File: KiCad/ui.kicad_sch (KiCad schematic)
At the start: 42 parts, among them SW1 PEC11R-4215F-S0024, SW2 PEC11R-4215F-S0024, U10 BME280, U11 SN74HC14PWR, U12 LM35DGS, U8 SN74AHCT244DBR, U9 24LC256-I_ST

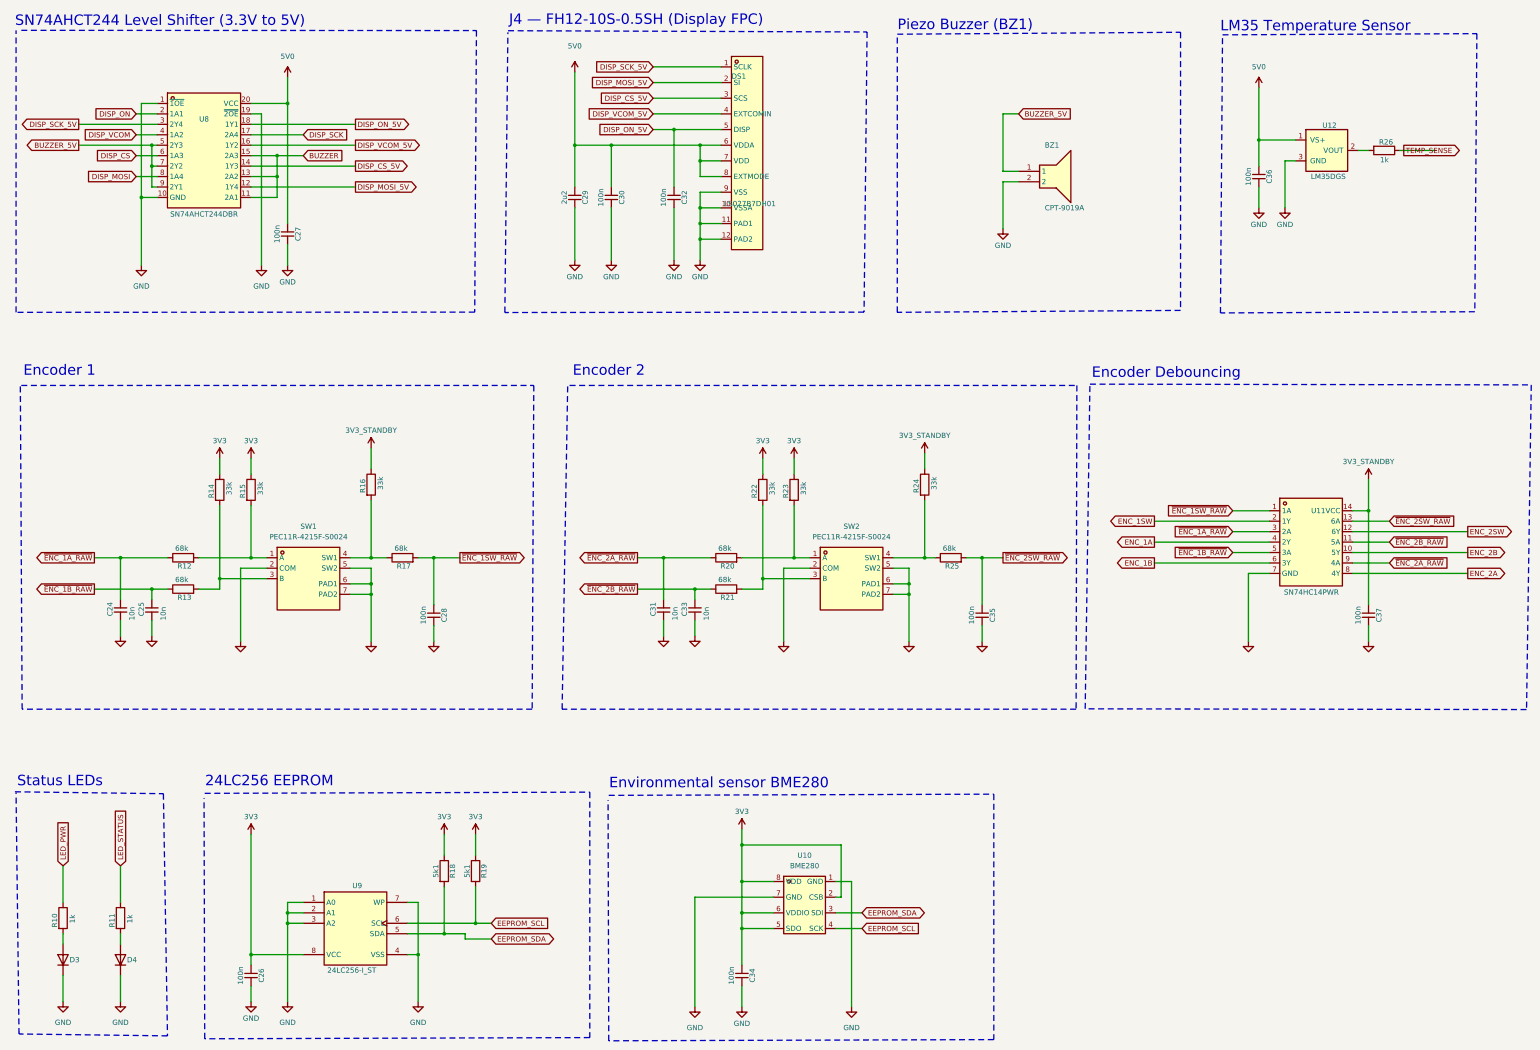
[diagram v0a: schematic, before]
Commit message: Symbols and board updated to match library
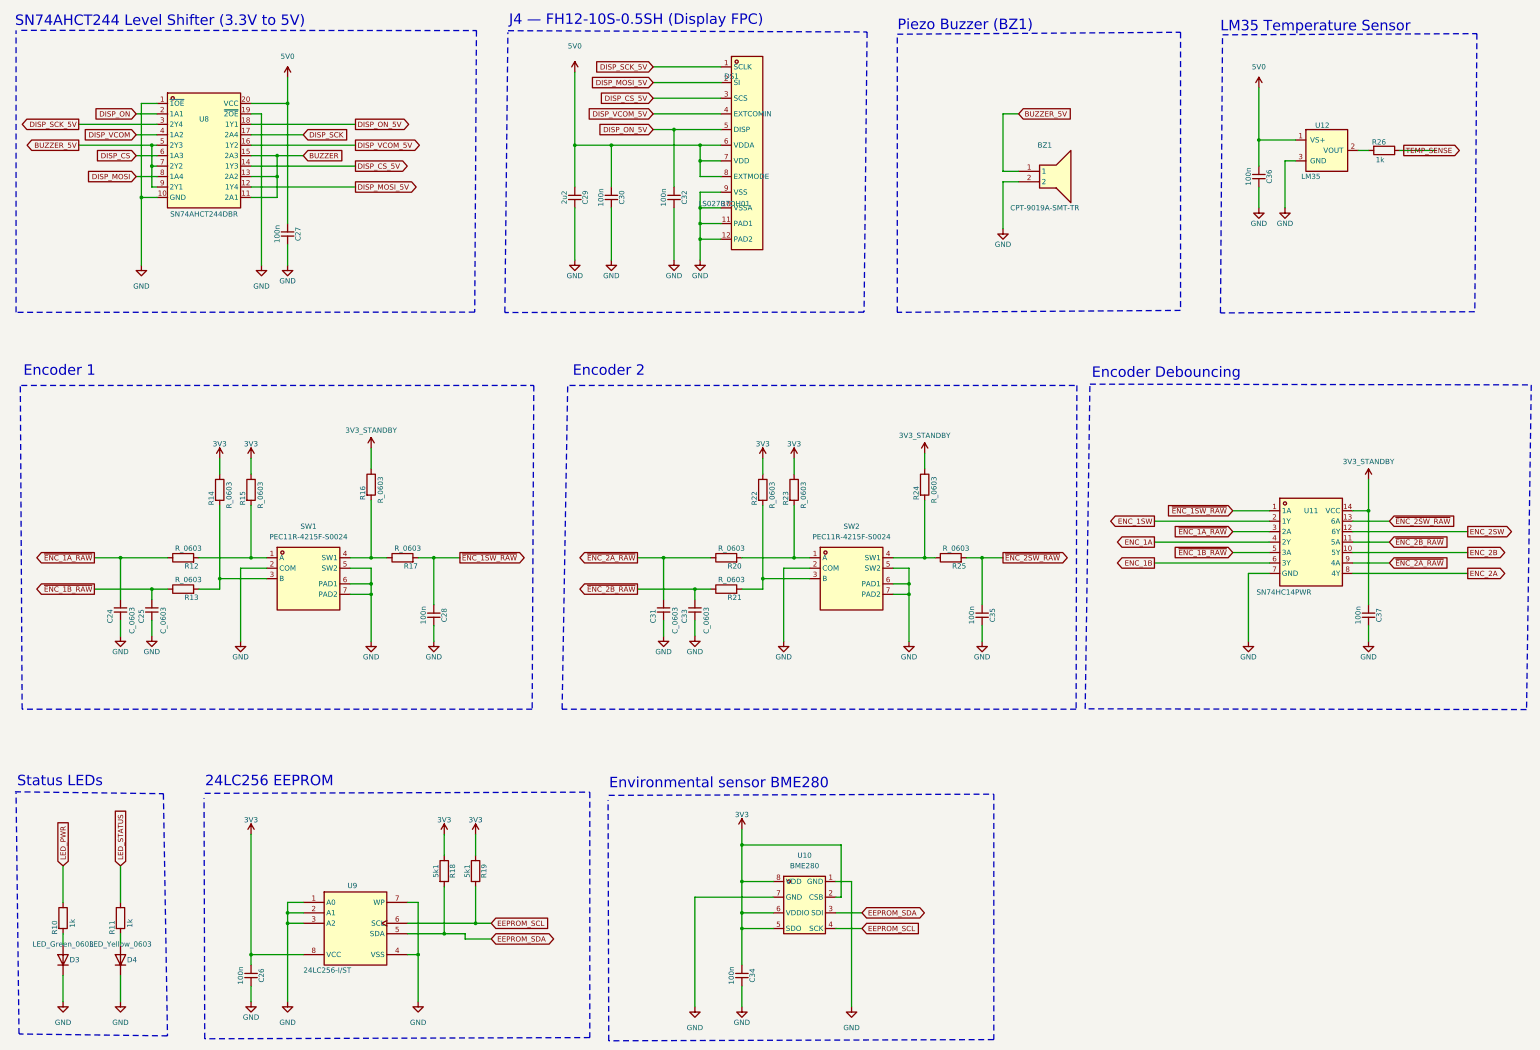
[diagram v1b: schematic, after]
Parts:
- BZ1: value CPT-9019A -> CPT-9019A-SMT-TR
- C24, C25, C31, C33: value 10n -> C_0603
- D4: value LED_Green_0603 -> LED_Yellow_0603
- R12, R13, R17, R20, R21, R25: value 68k -> R_0603
- R14, R15, R16, R22, R23, R24: value 33k -> R_0603
- U12: value LM35DGS -> LM35
- U9: value 24LC256-I_ST -> 24LC256-I/ST

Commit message: Remaining resistors and capacitors replaced by specific value components
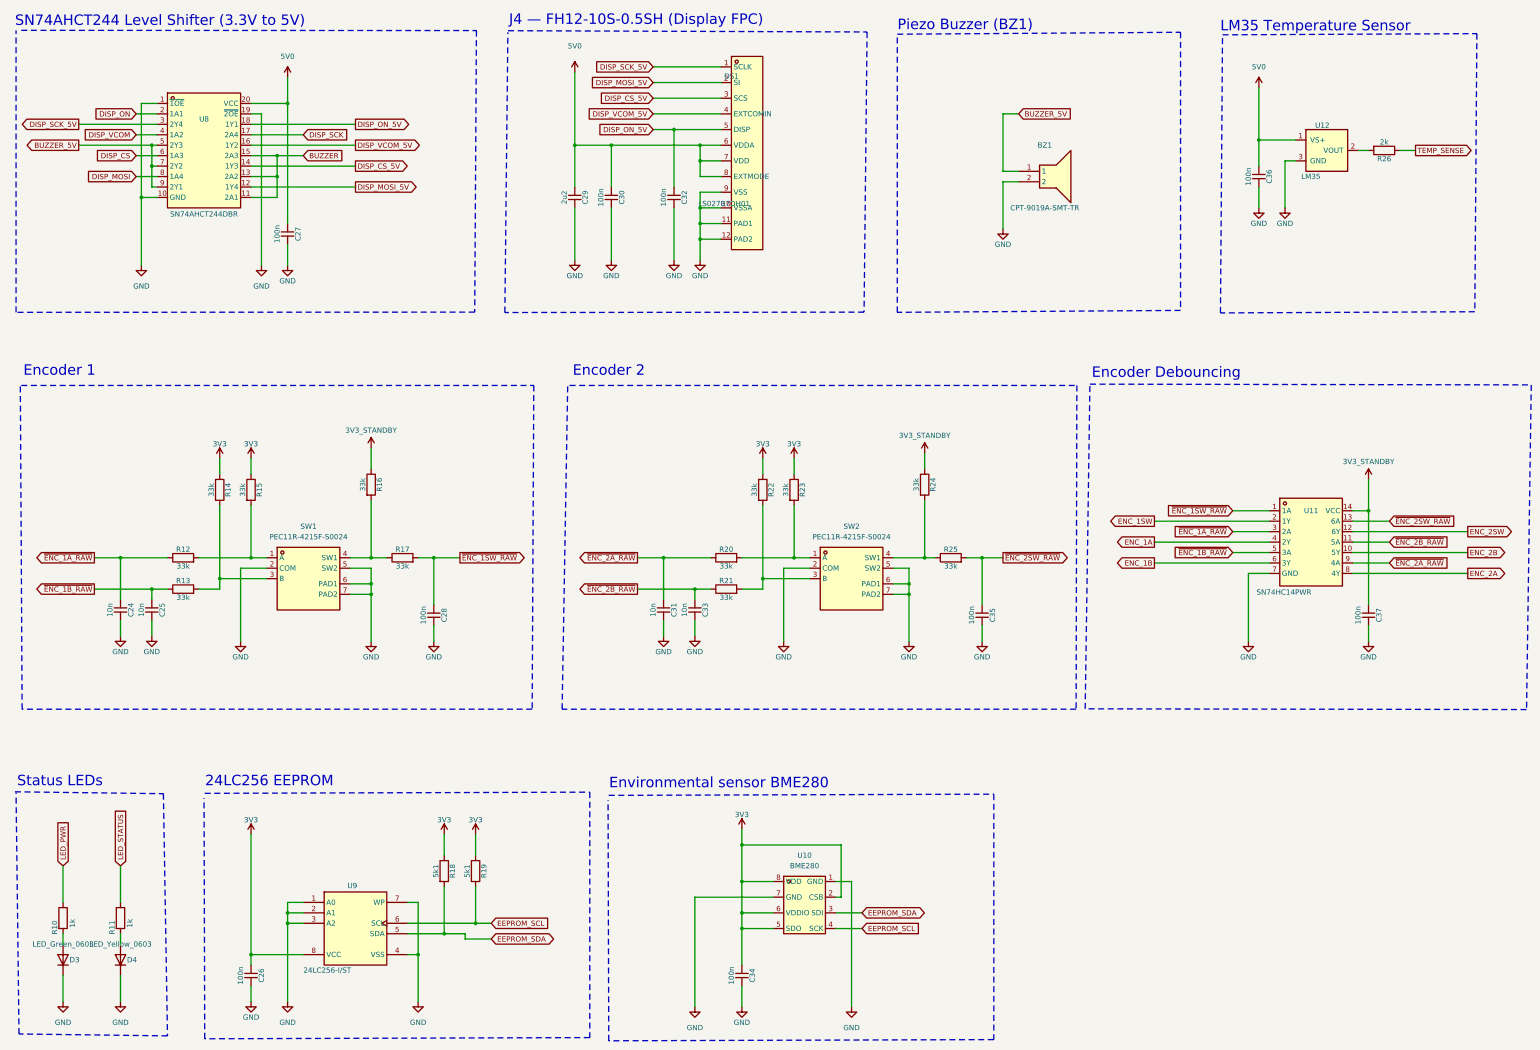
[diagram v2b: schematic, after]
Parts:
- C24, C25, C31, C33: value C_0603 -> 10n; symbol sldrnrd:Capacitor/C_0603 -> sldrnrd:Capacitor/C0603_10n; Dielectric (none) -> X7R; LCSC (none) -> C57112; MPN (none) -> 0603B103K500NT; Manufacturer (none) -> Fenghua; Voltage (none) -> 50V
- R12, R13, R14, R15, R16, R17, R20, R21, R22, R23, R24, R25: value R_0603 -> 33k; symbol sldrnrd:Resistor/R_0603 -> sldrnrd:Resistor/R0603_33k; LCSC (none) -> C4216; MPN (none) -> 0603WAF3302T5E; Manufacturer (none) -> Uni-Royal
- R26: value 1k -> 2k; symbol sldrnrd:Resistor/R0603_1k -> sldrnrd:Resistor/R0603_2k; LCSC C21190 -> C22975; MPN 0603WAF1001T5E -> 0603WAF2001T5E
